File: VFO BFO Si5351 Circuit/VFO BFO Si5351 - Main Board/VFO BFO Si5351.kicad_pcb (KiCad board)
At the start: 2 copper layers, 126 x 59.5 mm, 34 parts, among them J1 I2C Bus, J10 VIN +12V, J11 GND +5V +9V +12, J12 VFO_Front_Pannel, J2 Band, J3 Mode, J4 AGC, J5 ATT, J6 BFO, J7 TX, J8 IN RTTY, J9 IN S_meter, M1 Si5351A module, U1 ESP32-DEVKITC-32D, U2 PCF8574AP, U3 LM7809, U4 LM7805, U5 24LC32

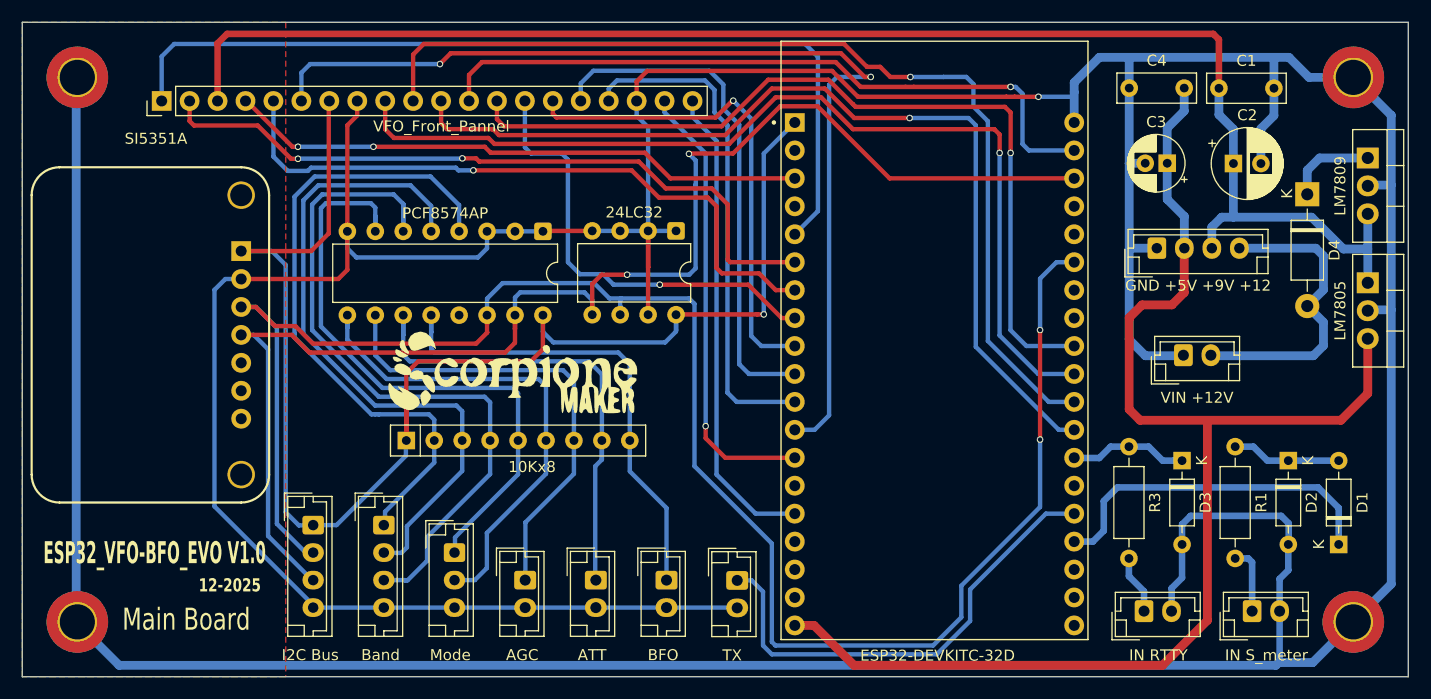
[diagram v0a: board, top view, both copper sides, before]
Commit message: Mod code end PCB
Schema elettrico Main-board and Front-panel correzione impronta SI5351 e PCB
Pulizia Codice ed implementazione out digitale  BFO
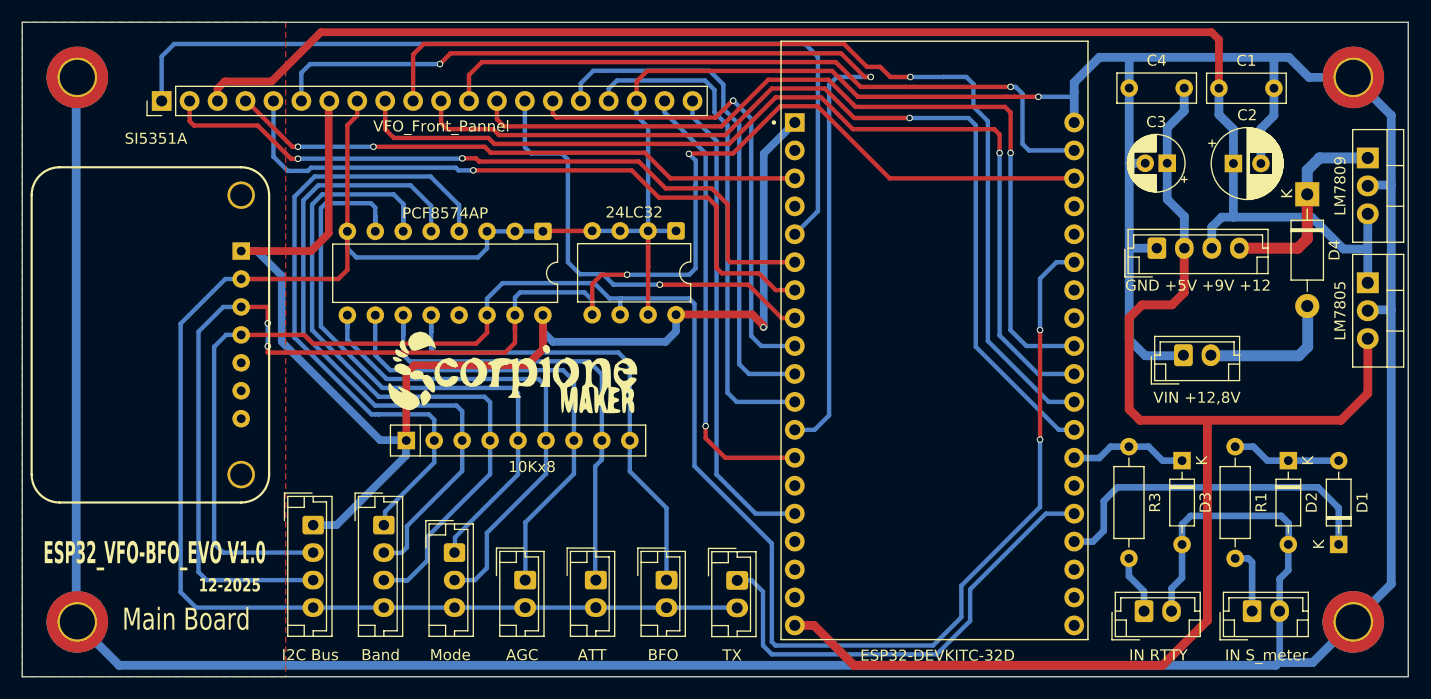
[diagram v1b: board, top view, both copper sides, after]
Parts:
- J10: value VIN +12V -> VIN +12,8V
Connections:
- D4 pad 1: Net-(D4-K) -> +12V
- D4 pad 2: +12V -> Net-(D4-A)
- J10 pad 2: +12V -> Net-(D4-A)
- M1 pad 3: SCL -> SDA
- M1 pad 4: SDA -> SCL
- U3 pad 1: Net-(D4-K) -> +12V
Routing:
- net SDA: track 128.9 -> 144.0 mm, vias 2 -> 4
- net Net-(D4-A): track 0.00 -> 12.9 mm
- net +12V: track 27.9 -> 18.7 mm
- net GND: track 536.0 -> 544.8 mm
- net Net-(D4-K): track 8.15 -> 0.00 mm
- net SCL: track 166.5 -> 170.0 mm
- net +3.3V: track 133.4 -> 130.7 mm
- net +9V: track 137.6 -> 135.3 mm
